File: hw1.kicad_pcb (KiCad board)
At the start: 2 copper layers, 92 x 50 mm, 63 parts, among them J1 USB_C_Receptacle_USB2.0_16P, J2 USB_C_Receptacle_USB2.0_16P, M1 Stepper_Motor, Q1 STL6P3LLH6, Q2 STL6P3LLH6, SW1 RotaryEncoder_Switch, SW2 SW_Back, SW3 SW_Bolus, SW4 SW_Settings, SW5 SW_Push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

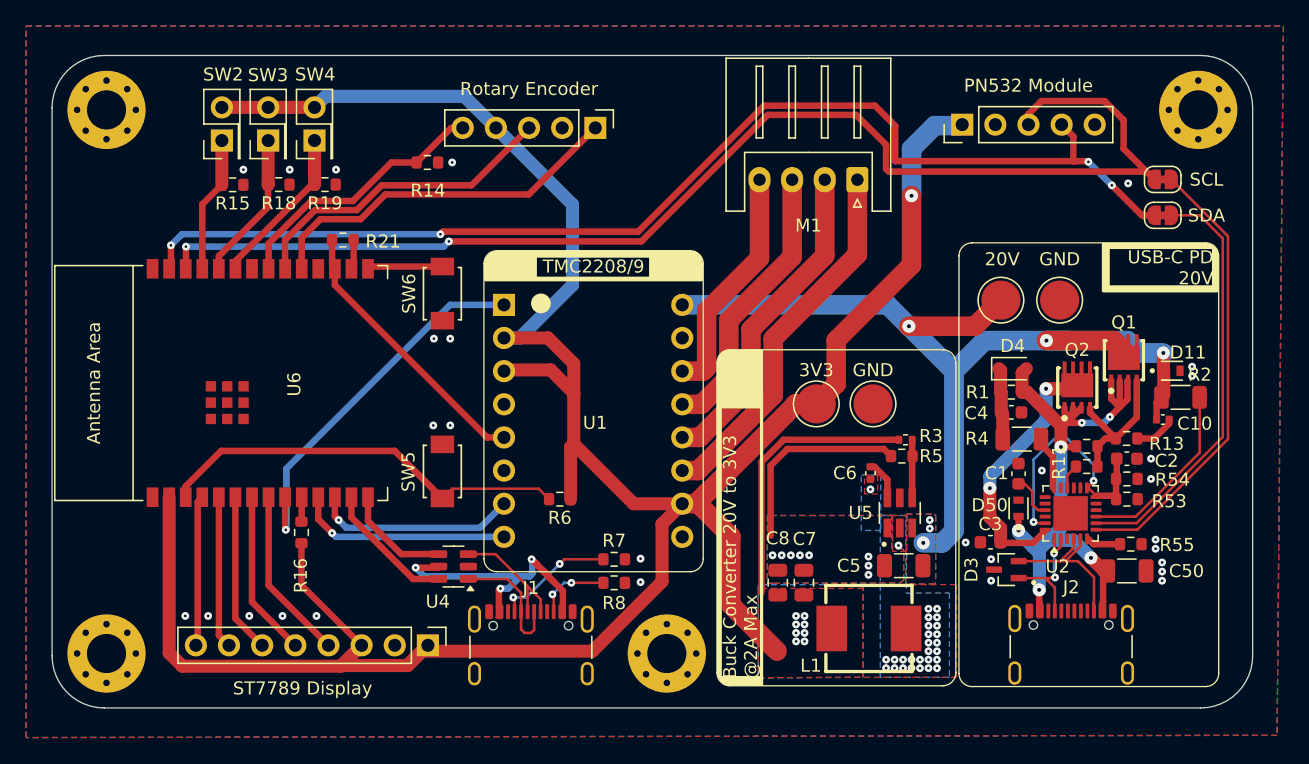
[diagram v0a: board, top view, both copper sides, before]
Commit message: Added LCSC codes, swapped extended components for basic ones, fixed labels and tidied schematics.
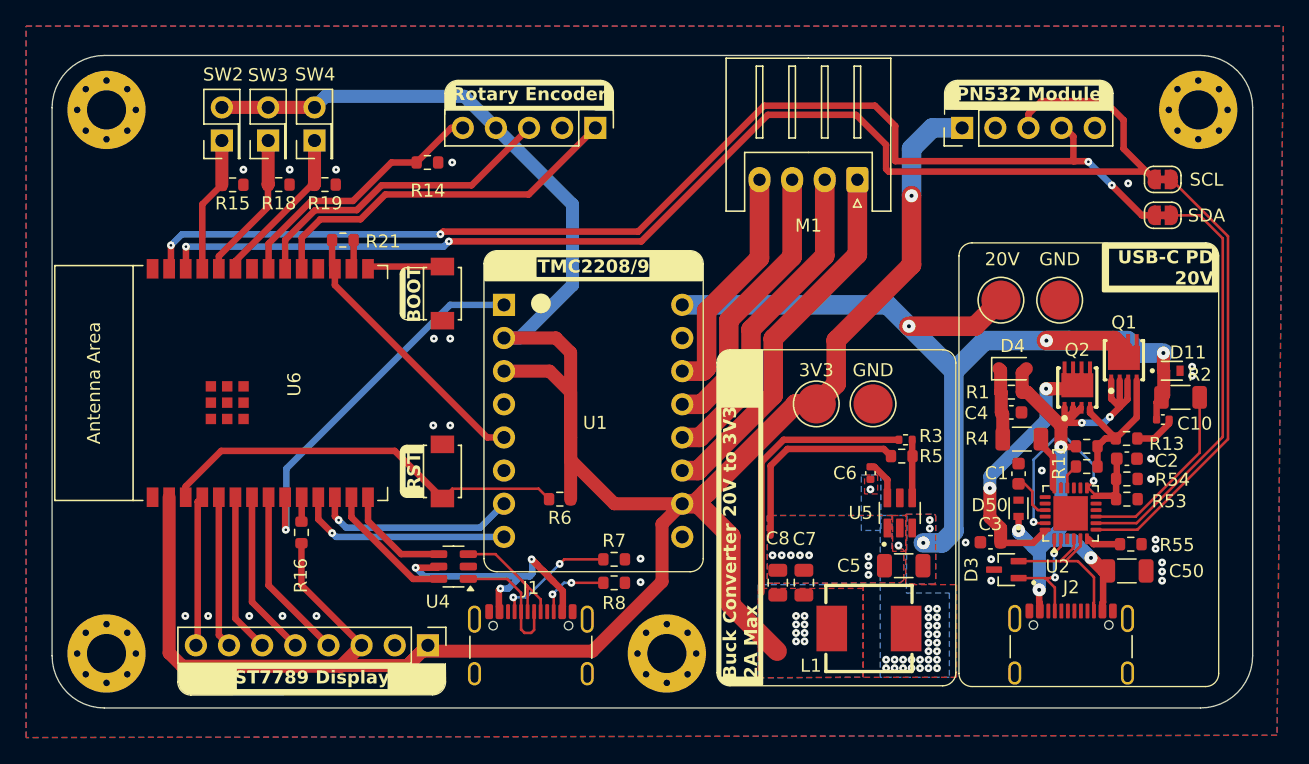
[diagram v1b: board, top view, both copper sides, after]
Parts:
- added REF**: Overture_title, hw1_footprint:Overture_title, B.Cu at (181.4, 110.3)
- added REF**: overture_logo, hw1_footprint:overture_logo, B.Cu at (181.7, 123.4)
- moved PN532-Module1 0.25 mm to (163.8, 83.6)
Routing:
- net +3.3_BUCK: track 226.2 -> 230.9 mm
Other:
- board text added: "BK"
- board text added: "BOOT"
- board text added: "Buck Converter 20V to 3V3 2A Max"
- board text added: "CLK"
- board text added: "CS"
- board text added: "DAT"
- board text added: "DC"
- board text added: "DIR"
- board text added: "EN"
- board text added: "ENC_A"
- board text added: "ENC_B"
- board text added: "ENC_S1"
- board text added: "ENC_S2"
- board text added: "I2C_SCL"
- board text added: "I2C_SDA"
- board text added: "M1A"
- board text added: "M1B"
- board text added: "M2A"
- board text added: "M2B"
- board text added: "MS1"
- board text added: "MS2"
- board text added: "NFC_IRQ"
- board text added: "PDN"
- board text added: "RST"
- board text added: "STEP"
- board text added: "SW"
- board text added: "UART"
- board text added: "VCC"
- board text added: "VIO"
- board text added: "VM"
- board text removed: "Buck Converter 20V to 3V3 @2A Max"

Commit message: Finalised design, sent PCB to manufacturing
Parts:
- moved REF** 76.4 mm to (107.8, 89.6), turned to 180 degrees
- moved REF** 69.6 mm to (121.0, 89.2), turned to 180 degrees
- moved JP5 2.75 mm to (179.2, 87.5)
- moved JP6 2.75 mm to (179.2, 90.3)
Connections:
- net /Sheet_Power/SW_TPS renamed /Power/SW_TPS
- JP5 pad 1: SDA -> SCL
- JP6 pad 1: SCL -> SDA
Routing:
- net VBUS: track 50.3 -> 45.4 mm
- net CC2: track 13.2 -> 11.5 mm
- net +3.3_BUCK: track 230.9 -> 229.6 mm
- net I2C_SCL: track 89.9 -> 88.7 mm, vias 4 -> 2
- net M2B: track 28.7 -> 29.7 mm
- net M2A: track 25.2 -> 26.2 mm
- net M1B: track 21.7 -> 22.7 mm
- net M1A: track 18.2 -> 19.2 mm
- net +20_USB: track 77.1 -> 78.1 mm
- net CC1: track 9.96 -> 9.14 mm
- net I2C_SDA: track 97.0 -> 96.8 mm, vias 2 -> 3
- net GND: vias 37 -> 36
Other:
- board text added: "GPIO"
- board text removed: "SW"
